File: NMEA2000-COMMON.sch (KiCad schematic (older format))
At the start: 55 parts, among them J2 CAN, SW1 PRG, SW2 INSTANCE, SW3 BUS, U1 MCP2551-I-P, U2 TMR-2-2411, U3 74HCT595, U4 74HCT595, U5 Teensy_4.0

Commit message: Update silk layer.
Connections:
- net 3V3 renamed +3V3
- no-connect marks 9 -> 17
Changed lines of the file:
@@
 Text Label 8650 5000 2    50   ~ 0
 MPX_SER
-Text Label 1150 3500 2    50   ~ 0
-3V3
 $Comp
 L Device:CP_Small C3
@@
 Text Label 2250 3500 0    50   ~ 0
 MPX_LATCH
-Text Label 1150 2700 2    50   ~ 0
-CH7
 Text Label 1150 2800 2    50   ~ 0
 CH6
@@
 	-1   0    0    -1
 $EndComp
+$Comp
+L power:+3V3 #PWR0103
+U 1 1 639236D5
+P 850 3500
+F 0 "#PWR0103" H 850 3350 50  0001 C CNN
+F 1 "+3V3" H 865 3673 50  0000 C CNN
+F 2 "" H 850 3500 50  0001 C CNN
+F 3 "" H 850 3500 50  0001 C CNN
+	1    850  3500
+	1    0    0    -1
+$EndComp
+Wire Wire Line
+	1150 3500 850  3500
+Text Label 1150 2700 2    50   ~ 0
+CH7
+NoConn ~ 1150 2700
+NoConn ~ 1150 2800
+NoConn ~ 1150 2900
+NoConn ~ 1150 3000
+NoConn ~ 1150 3100
+NoConn ~ 1150 3200
+NoConn ~ 1150 3300
+NoConn ~ 1150 3400
 $EndSCHEMATC

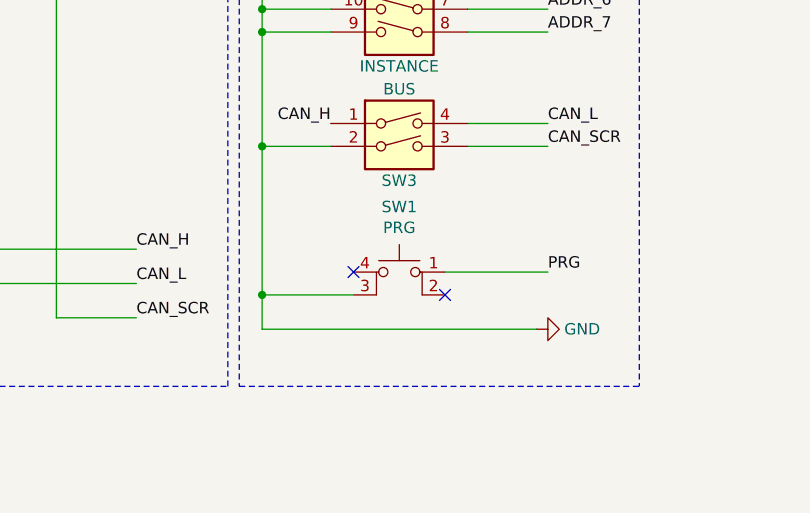
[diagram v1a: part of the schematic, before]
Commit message: Update PRG switch position
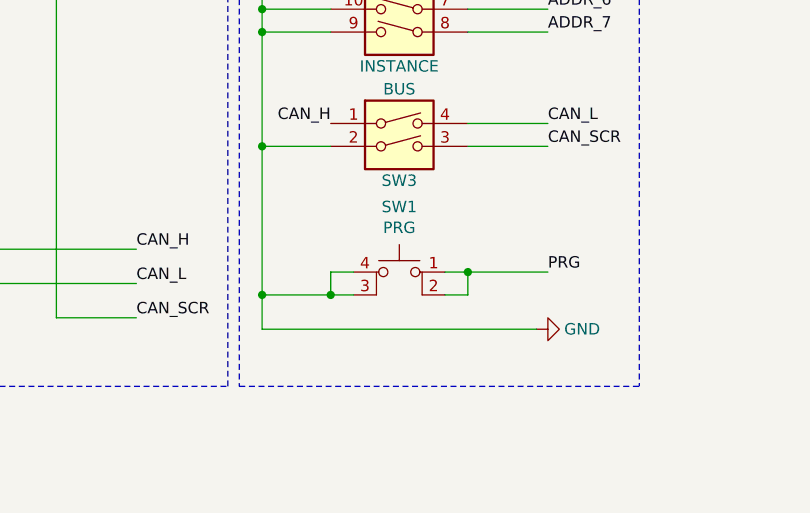
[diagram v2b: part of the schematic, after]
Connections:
- net GND: now also SW1.4 (A)
- net PRG: now also SW1.2
- no-connect marks 17 -> 15
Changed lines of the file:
@@
 	1200 6700 2350 6700
 Wire Wire Line
-	5950 7150 6400 7150
+	5950 7150 6050 7150
 Wire Wire Line
 	5150 7400 6350 7400
@@
 	-1   0    0    -1
 $EndComp
-NoConn ~ 5950 7250
-NoConn ~ 5550 7150
-Wire Wire Line
-	5550 7250 5150 7250
+Wire Wire Line
+	5550 7250 5450 7250
 $Comp
 L Device:LED D18
@@
 NoConn ~ 1150 3300
 NoConn ~ 1150 3400
+Wire Wire Line
+	5950 7250 6050 7250
+Wire Wire Line
+	6050 7250 6050 7150
+Connection ~ 6050 7150
+Wire Wire Line
+	6050 7150 6400 7150
+Wire Wire Line
+	5550 7150 5450 7150
+Wire Wire Line
+	5450 7150 5450 7250
+Connection ~ 5450 7250
+Wire Wire Line
+	5450 7250 5150 7250
 $EndSCHEMATC

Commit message: Revise INSTANCE
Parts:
- added C?: 100nF, Capacitor_SMD:C_0805_2012Metric, symbol Device:CP_Small
- added U?: 74LS165, symbol pdjr:74LS165
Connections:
- net labels added: D16, D17, D18, D19, D20, D21, D22, D23, D5, D6, D7, D8, INSTANCE_CLOCK, INSTANCE_CLOCK_ENABLE, INSTANCE_LOAD, INSTANCE_SERIAL, LED_CLOCK, LED_DATA, LED_LATCH, LED_SER
- net labels removed: CH0, CH1, CH2, CH3, CH4, CH5, CH6, CH7, MPX_CLOCK, MPX_DATA, MPX_LATCH, MPX_SER
- wire segments 205 -> 240
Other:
- moved on the sheet: SW2
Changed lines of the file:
@@
 	10350 3800 10450 3800
 Text Label 8650 3300 2    50   ~ 0
-MPX_DATA
+LED_DATA
 Text Label 8650 3500 2    50   ~ 0
-MPX_CLOCK
+LED_CLOCK
 Text Label 8650 3800 2    50   ~ 0
-MPX_LATCH
+LED_LATCH
 Wire Wire Line
 	9250 4400 9250 4500
@@
 L Switch:SW_DIP_x08 SW2
 U 1 1 633236F9
-P 5750 5800
-F 0 "SW2" H 5750 6350 50  0000 C CNN
-F 1 "INSTANCE" H 5750 5350 50  0000 C CNN
-F 2 "Package_DIP:DIP-16_W7.62mm" H 5750 5800 50  0001 C CNN
-F 3 "~" H 5750 5800 50  0001 C CNN
-	1    5750 5800
-	-1   0    0    -1
+P 6350 2000
+F 0 "SW2" H 6350 2550 50  0000 C CNN
+F 1 "INSTANCE" H 6350 1550 50  0000 C CNN
+F 2 "Package_DIP:DIP-16_W7.62mm" H 6350 2000 50  0001 C CNN
+F 3 "~" H 6350 2000 50  0001 C CNN
+	1    6350 2000
+	1    0    0    -1
 $EndComp
 Wire Wire Line
@@
 NoConn ~ 9650 5900
 Text Label 8650 5200 2    50   ~ 0
-MPX_CLOCK
+LED_CLOCK
 Text Label 8650 5500 2    50   ~ 0
-MPX_LATCH
+LED_LATCH
 Wire Wire Line
 	9250 6100 9250 6200
@@
 	10950 4000 10950 4500
 Text Label 9650 4200 0    50   ~ 0
-MPX_SER
+LED_SER
 Text Label 8650 5000 2    50   ~ 0
-MPX_SER
+LED_SER
 $Comp
 L Device:CP_Small C3
@@
 PRG
 Text Label 2250 3600 0    50   ~ 0
-MPX_CLOCK
+LED_CLOCK
 Text Label 2250 3400 0    50   ~ 0
-MPX_DATA
-Text Label 2250 3100 0    50   ~ 0
-ADDR_7
-Text Label 2250 3000 0    50   ~ 0
-ADDR_6
-Text Label 2250 2900 0    50   ~ 0
-ADDR_5
-Text Label 2250 2800 0    50   ~ 0
-ADDR_4
-Text Label 2250 2700 0    50   ~ 0
-ADDR_3
-Text Label 2250 2600 0    50   ~ 0
-ADDR_2
-Text Label 2250 2500 0    50   ~ 0
-ADDR_1
-Text Label 2250 2400 0    50   ~ 0
-ADDR_0
+LED_DATA
 Text Label 2250 3500 0    50   ~ 0
-MPX_LATCH
+LED_LATCH
 Text Label 1150 2800 2    50   ~ 0
-CH6
+D17
 Text Label 1150 2900 2    50   ~ 0
-CH5
+D18
 Text Label 1150 3000 2    50   ~ 0
-CH4
+D19
 Text Label 1150 3100 2    50   ~ 0
-CH3
+D20
 Text Label 1150 3200 2    50   ~ 0
-CH2
+D21
 Text Label 1150 3300 2    50   ~ 0
-CH1
+D22
 Text Label 1150 3400 2    50   ~ 0
-CH0
+D23
 NoConn ~ 1500 2200
 NoConn ~ 1600 2200
@@
 	1150 3500 850  3500
 Text Label 1150 2700 2    50   ~ 0
-CH7
+D16
 NoConn ~ 1150 2700
 NoConn ~ 1150 2800
@@
 Wire Wire Line
 	5450 7250 5150 7250
+Wire Wire Line
+	4100 1500 4000 1500
+Wire Wire Line
+	4600 1100 4150 1100
+$Comp
+L power:+3V3 #PWR?
+U 1 1 63A6B75E
+P 4150 1100
+F 0 "#PWR?" H 4150 950 50  0001 C CNN
+F 1 "+3V3" V 4150 1300 50  0000 C CNN
+F 2 "" H 4150 1100 50  0001 C CNN
+F 3 "" H 4150 1100 50  0001 C CNN
+	1    4150 1100
+	0    -1   -1   0
+$EndComp
+$Comp
+L power:GND #PWR?
+U 1 1 63A6CC25
+P 3950 2600
+F 0 "#PWR?" H 3950 2350 50  0001 C CNN
+F 1 "GND" V 3950 2400 50  0000 C CNN
+F 2 "" H 3950 2600 50  0001 C CNN
+F 3 "" H 3950 2600 50  0001 C CNN
+	1    3950 2600
+	0    1    1    0
+$EndComp
+Wire Wire Line
+	5100 1600 5200 1600
+Wire Wire Line
+	5100 1700 5200 1700
+Wire Wire Line
+	5100 1800 5200 1800
+Wire Wire Line
+	5100 1900 5200 1900
+Wire Wire Line
+	5100 2000 5200 2000
+Wire Wire Line
+	5100 2100 5200 2100
+Wire Wire Line
+	5100 2200 5200 2200
+Wire Wire Line
+	5100 2300 5200 2300
+Wire Wire Line
+	6750 2300 6650 2300
+Wire Wire Line
+	6750 2300 6750 2200
+Wire Wire Line
+	6750 2200 6650 2200
+Connection ~ 6750 2300
+Wire Wire Line
+	6750 2200 6750 2100
+Wire Wire Line
+	6750 2100 6650 2100
+Connection ~ 6750 2200
+Wire Wire Line
+	6750 2100 6750 2000
+Wire Wire Line
+	6750 2000 6650 2000
+Connection ~ 6750 2100
+Wire Wire Line
+	6750 2000 6750 1900
+Wire Wire Line
+	6750 1900 6650 1900
+Connection ~ 6750 2000
+Wire Wire Line
+	6750 1900 6750 1800
+Wire Wire Line
+	6750 1800 6650 1800
+Connection ~ 6750 1900
+Wire Wire Line
+	6750 1800 6750 1700
+Wire Wire Line
+	6750 1700 6650 1700
+Connection ~ 6750 1800
+Wire Wire Line
+	6750 1700 6750 1600
+Wire Wire Line
+	6750 1600 6650 1600
+Connection ~ 6750 1700
+$Comp
+L Device:CP_Small C?
+U 1 1 63C82001
+P 5150 1100
+F 0 "C?" V 5200 1200 50  0000 C CNN
+F 1 "100nF" V 5200 950 50  0000 C CNN
+F 2 "Capacitor_SMD:C_0805_2012Metric" H 5150 1100 50  0001 C CNN
+F 3 "~" H 5150 1100 50  0001 C CNN
+	1    5150 1100
+	0    -1   1    0
+$EndComp
+Wire Wire Line
+	6750 1600 6750 1100
+Wire Wire Line
+	5900 1100 5250 1100
+Connection ~ 6750 1600
+Wire Wire Line
+	5050 1100 4600 1100
+Connection ~ 4600 1100
+Wire Wire Line
+	4600 1100 4600 1200
+$Comp
+L pdjr:74LS165 U?
+U 1 1 63F7C7A4
+P 4600 2100
+F 0 "U?" H 4850 2850 50  0000 C CNN
+F 1 "74LS165" H 4300 2850 50  0000 C CNN
+F 2 "" H 4600 2100 50  0001 C CNN
+F 3 "https://www.ti.com/lit/ds/symlink/sn74ls165a.pdf" H 4600 2100 50  0001 C CNN
+	1    4600 2100
+	-1   0    0    -1
+$EndComp
+Wire Wire Line
+	4600 2600 5900 2550
+Wire Wire Line
+	6750 2600 6750 2300
+Wire Wire Line
+	3950 2600 4600 2600
+Connection ~ 4600 2600
+Text Label 4000 2000 2    50   ~ 0
+INSTANCE_CLOCK
+Text Label 4000 1500 2    50   ~ 0
+INSTANCE_SERIAL
+Wire Wire Line
+	4100 2000 4000 2000
+Text Label 4000 2100 2    50   ~ 0
+INSTANCE_CLOCK_ENABLE
+Wire Wire Line
+	4100 2100 4000 2100
+Text Label 4000 1800 2    50   ~ 0
+INSTANCE_LOAD
+Wire Wire Line
+	4100 1800 4000 1800
+Text Label 2250 2400 0    50   ~ 0
+INSTANCE_LOAD
+Text Label 2250 2500 0    50   ~ 0
+INSTANCE_CLOCK
+Text Label 2250 2600 0    50   ~ 0
+INSTANCE_SERIAL
+Text Label 2250 2700 0    50   ~ 0
+INSTANCE_CLOCK_ENABLE
+Text Label 2250 2800 0    50   ~ 0
+D8
+Text Label 2250 2900 0    50   ~ 0
+D7
+Text Label 2250 3000 0    50   ~ 0
+D6
+Text Label 2250 3100 0    50   ~ 0
+D5
 $EndSCHEMATC

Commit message: PISI update
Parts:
- added R101, R102, R103, R104, R105, R106, R107, R108: 4K7 0.125W, Resistor_SMD:R_0805_2012Metric, symbol Device:R
- U101: renamed from U?; footprint (none) -> Package_SO:SO-16_3.9x9.9mm_P1.27mm
- gave numbers to parts that had none: 1
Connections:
- net labels added: INSTANCE_CE, INSTANCE_CP, INSTANCE_PL, INSTANCE_Q7
- net labels removed: ADDR_0, ADDR_1, ADDR_2, ADDR_3, ADDR_4, ADDR_5, ADDR_6, ADDR_7, INSTANCE_CLOCK, INSTANCE_CLOCK_ENABLE, INSTANCE_LOAD, INSTANCE_SERIAL
- wire segments 240 -> 250
- no-connect marks 15 -> 19
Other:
- moved on the sheet: C101, SW2, U101

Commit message: Tidy up
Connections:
- net GND: now also SW3.4; no longer SW3.2
- net CAN_H: no longer names the net of SW3.1
- net CAN_H: now also J2.5 (Pin_5); no longer R2.2
- net CAN_L: no longer names the net of J2.4 (Pin_4), U1.6 (CANL)
- net CAN_L: now also SW3.3; no longer SW3.4
- removed net CAN_SCR: J2.5 (Pin_5), SW3.3
- new net: R2.2, SW3.2
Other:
- note removed: "CONFIGURATION"
- moved on the sheet: R2, SW1, SW3
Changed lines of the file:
@@
 Text Label 650  7100 0    50   ~ 0
 CAN_TX
-Wire Wire Line
-	4250 7350 4600 7350
 Text Notes 600  5200 0    50   ~ 10
 POWER SUPPLY & CAN INTERFACE
-Text Label 4600 7350 0    50   ~ 0
-CAN_SCR
 Wire Wire Line
 	3350 5800 3450 5800
@@
 L Device:R R2
 U 1 1 63360130
-P 3800 7050
-F 0 "R2" V 3700 7100 50  0000 R CNN
-F 1 "120R 0.5W" V 3800 7050 20  0000 C CNN
-F 2 "Resistor_THT:R_Axial_DIN0207_L6.3mm_D2.5mm_P7.62mm_Horizontal" V 3730 7050 50  0001 C CNN
-F 3 "~" H 3800 7050 50  0001 C CNN
-	1    3800 7050
-	0    -1   -1   0
-$EndComp
-Text Label 4600 7050 0    50   ~ 0
-CAN_H
-Wire Wire Line
-	4600 7050 3950 7050
-Text Label 4600 7200 0    50   ~ 0
-CAN_L
-Wire Wire Line
-	3350 6700 3550 6700
-Wire Wire Line
-	3650 7050 3550 7050
-Wire Wire Line
-	3550 7050 3550 6700
-Connection ~ 3550 6700
-Wire Wire Line
-	3550 6700 3900 6700
-Wire Wire Line
-	4600 7200 3450 7200
-Wire Wire Line
-	3450 7200 3450 6900
-Connection ~ 3450 6900
-Wire Wire Line
-	3450 6900 4000 6900
-Wire Wire Line
-	3350 6900 3450 6900
-Text Label 5450 6500 2    50   ~ 0
-CAN_H
-Text Label 6400 6500 0    50   ~ 0
-CAN_L
+P 4000 6700
+F 0 "R2" V 3900 6750 50  0000 R CNN
+F 1 "120R 0.5W" V 4000 6700 20  0000 C CNN
+F 2 "Resistor_THT:R_Axial_DIN0207_L6.3mm_D2.5mm_P7.62mm_Horizontal" V 3930 6700 50  0001 C CNN
+F 3 "~" H 4000 6700 50  0001 C CNN
+	1    4000 6700
+	0    -1   -1   0
+$EndComp
 $Comp
 L Connector:Screw_Terminal_01x05 J2
@@
 	-1   0    0    1
 $EndComp
-Text Label 6400 6600 0    50   ~ 0
-CAN_SCR
 $Comp
 L Switch:SW_DIP_x02 SW3
 U 1 1 62A67242
-P 5750 6600
-F 0 "SW3" H 5750 6450 50  0000 C CNN
-F 1 "BUS" H 5750 6850 50  0000 C CNN
-F 2 "Package_DIP:DIP-4_W7.62mm_LongPads" H 5750 6600 50  0001 C CNN
-F 3 "~" H 5750 6600 50  0001 C CNN
-	1    5750 6600
+P 4550 6700
+F 0 "SW3" H 4550 6550 50  0000 C CNN
+F 1 "BUS" H 4550 6950 50  0000 C CNN
+F 2 "Package_DIP:DIP-4_W7.62mm_LongPads" H 4550 6700 50  0001 C CNN
+F 3 "~" H 4550 6700 50  0001 C CNN
+	1    4550 6700
 	1    0    0    -1
 $EndComp
@@
 	1    0    0    -1
 $EndComp
-Wire Wire Line
-	5150 6600 5450 6600
 Connection ~ 9250 3000
 Wire Wire Line
@@
 Wire Wire Line
 	10000 3000 10950 3000
-Text Label 6400 7150 0    50   ~ 0
+Text Label 6600 3250 2    50   ~ 0
 PRG
 $Comp
@@
 Wire Wire Line
 	950  5800 2000 5800
-Wire Notes Line
-	5050 5200 6800 5200
-Text Notes 5050 5200 0    50   ~ 10
-CONFIGURATION
 Wire Notes Line
 	11050 2400 11050 6350
@@
 Wire Notes Line
 	600  7650 5000 7650
-Wire Notes Line
-	5050 7650 6800 7650
-Wire Notes Line
-	6800 5200 6800 7650
-Wire Notes Line
-	5050 5200 5050 7650
 $Comp
 L power:GND #PWR014
 U 1 1 63724529
-P 6350 7400
-F 0 "#PWR014" H 6350 7150 50  0001 C CNN
-F 1 "GND" V 6350 7200 50  0000 C CNN
-F 2 "" H 6350 7400 50  0001 C CNN
-F 3 "" H 6350 7400 50  0001 C CNN
-	1    6350 7400
-	0    -1   -1   0
-$EndComp
-Wire Wire Line
-	6050 6500 6400 6500
-Wire Wire Line
-	6050 6600 6400 6600
+P 4600 3550
+F 0 "#PWR014" H 4600 3300 50  0001 C CNN
+F 1 "GND" V 4600 3350 50  0000 C CNN
+F 2 "" H 4600 3550 50  0001 C CNN
+F 3 "" H 4600 3550 50  0001 C CNN
+	1    4600 3550
+	0    1    -1   0
+$EndComp
 NoConn ~ -3250 8100
 $Comp
@@
 	1200 6700 2350 6700
 Wire Wire Line
-	5950 7150 6050 7150
-Wire Wire Line
-	5150 7400 6350 7400
+	6800 3250 6700 3250
+Wire Wire Line
+	7450 3550 5300 3550
 Connection ~ 1400 7550
 Wire Wire Line
@@
 L Switch:SW_MEC_5E SW1
 U 1 1 638DE6DD
-P 5750 7250
-F 0 "SW1" H 5750 7635 50  0000 C CNN
-F 1 "PRG" H 5750 7544 50  0000 C CNN
-F 2 "Button_Switch_THT:SW_TH_Tactile_Omron_B3F-10xx" H 5750 7550 50  0001 C CNN
-F 3 "http://www.apem.com/int/index.php?controller=attachment&id_attachment=1371" H 5750 7550 50  0001 C CNN
-	1    5750 7250
-	-1   0    0    -1
-$EndComp
-Wire Wire Line
-	5550 7250 5450 7250
+P 7000 3350
+F 0 "SW1" H 7000 3600 50  0000 C CNN
+F 1 "PRG" H 7000 3350 50  0000 C CNN
+F 2 "Button_Switch_THT:SW_TH_Tactile_Omron_B3F-10xx" H 7000 3650 50  0001 C CNN
+F 3 "http://www.apem.com/int/index.php?controller=attachment&id_attachment=1371" H 7000 3650 50  0001 C CNN
+	1    7000 3350
+	1    0    0    -1
+$EndComp
 $Comp
 L Device:LED D18
@@
 	3850 5400 4350 5400
 Wire Wire Line
-	4350 5800 4250 5800
-Wire Wire Line
-	4250 5800 4250 7350
-Wire Wire Line
-	4350 5700 4000 5700
-Wire Wire Line
-	4000 5700 4000 6900
-Wire Wire Line
-	3900 5600 4350 5600
-Wire Wire Line
-	3900 5600 3900 6700
+	4350 5700 3750 5700
+Wire Wire Line
+	3750 5700 3750 6900
+Wire Wire Line
+	3650 5600 4350 5600
+Wire Wire Line
+	3650 5600 3650 6700
 Text Notes 4600 5450 0    50   ~ 0
 NET_S
@@
 Wire Wire Line
 	4600 5200 4650 5200
-Wire Wire Line
-	5150 6600 5150 7250
-Connection ~ 5150 7250
-Wire Wire Line
-	5150 7250 5150 7400
 $Comp
 L pdjr:TMR-2-2411 U2
@@
 NoConn ~ 1150 3400
 Wire Wire Line
-	5950 7250 6050 7250
-Wire Wire Line
-	6050 7250 6050 7150
-Connection ~ 6050 7150
-Wire Wire Line
-	6050 7150 6400 7150
-Wire Wire Line
-	5550 7150 5450 7150
-Wire Wire Line
-	5450 7150 5450 7250
-Connection ~ 5450 7250
-Wire Wire Line
-	5450 7250 5150 7250
+	6800 3350 6700 3350
+Wire Wire Line
+	6700 3350 6700 3250
+Connection ~ 6700 3250
+Wire Wire Line
+	6700 3250 6600 3250
 Wire Wire Line
 	4800 2000 4600 2000
 Wire Wire Line
-	5300 1600 4850 1600
-$Comp
-L power:GND #PWR0104
-U 1 1 63A6CC25
-P 4650 3300
-F 0 "#PWR0104" H 4650 3050 50  0001 C CNN
-F 1 "GND" V 4650 3100 50  0000 C CNN
-F 2 "" H 4650 3300 50  0001 C CNN
-F 3 "" H 4650 3300 50  0001 C CNN
-	1    4650 3300
-	0    1    1    0
-$EndComp
+	5300 1600 4600 1600
 Wire Wire Line
 	7450 2800 7300 2800
@@
 U 1 1 63C82001
 P 7000 1600
-F 0 "C101" V 7050 1700 50  0000 C CNN
+F 0 "C101" V 7050 1750 50  0000 C CNN
 F 1 "100nF" V 7050 1450 50  0000 C CNN
 F 2 "Capacitor_SMD:C_0805_2012Metric" H 7000 1600 50  0001 C CNN
@@
 U 1 1 6394A88D
 P 6000 1850
-F 0 "R102" H 6000 1700 50  0000 R CNN
+F 0 "R102" V 5950 2150 50  0000 R CNN
 F 1 "4K7 0.125W" V 6000 1850 20  0000 C CNN
 F 2 "Resistor_SMD:R_0805_2012Metric" V 5930 1850 50  0001 C CNN
@@
 U 1 1 6394F8BB
 P 6100 1850
-F 0 "R103" H 6100 1700 50  0000 R CNN
+F 0 "R103" V 6050 2150 50  0000 R CNN
 F 1 "4K7 0.125W" V 6100 1850 20  0000 C CNN
 F 2 "Resistor_SMD:R_0805_2012Metric" V 6030 1850 50  0001 C CNN
@@
 U 1 1 6395000A
 P 6200 1850
-F 0 "R104" H 6200 1700 50  0000 R CNN
+F 0 "R104" V 6150 2150 50  0000 R CNN
 F 1 "4K7 0.125W" V 6200 1850 20  0000 C CNN
 F 2 "Resistor_SMD:R_0805_2012Metric" V 6130 1850 50  0001 C CNN
@@
 U 1 1 63950611
 P 6300 1850
-F 0 "R105" H 6300 1700 50  0000 R CNN
+F 0 "R105" V 6250 2150 50  0000 R CNN
 F 1 "4K7 0.125W" V 6300 1850 20  0000 C CNN
 F 2 "Resistor_SMD:R_0805_2012Metric" V 6230 1850 50  0001 C CNN
@@
 U 1 1 63950BCD
 P 6400 1850
-F 0 "R106" H 6400 1700 50  0000 R CNN
+F 0 "R106" V 6350 2150 50  0000 R CNN
 F 1 "4K7 0.125W" V 6400 1850 20  0000 C CNN
 F 2 "Resistor_SMD:R_0805_2012Metric" V 6330 1850 50  0001 C CNN
@@
 U 1 1 639511BB
 P 6500 1850
-F 0 "R107" H 6500 1700 50  0000 R CNN
+F 0 "R107" V 6450 2150 50  0000 R CNN
 F 1 "4K7 0.125W" V 6500 1850 20  0000 C CNN
 F 2 "Resistor_SMD:R_0805_2012Metric" V 6430 1850 50  0001 C CNN
@@
 U 1 1 63951797
 P 6600 1850
-F 0 "R108" H 6600 1700 50  0000 R CNN
+F 0 "R108" V 6550 2150 50  0000 R CNN
 F 1 "4K7 0.125W" V 6600 1850 20  0000 C CNN
 F 2 "Resistor_SMD:R_0805_2012Metric" V 6530 1850 50  0001 C CNN
@@
 U 1 1 63B2611A
 P 5900 1850
-F 0 "R101" H 5900 1700 50  0000 R CNN
+F 0 "R101" V 5850 2150 50  0000 R CNN
 F 1 "4K7 0.125W" V 5900 1850 20  0000 C CNN
 F 2 "Resistor_SMD:R_0805_2012Metric" V 5830 1850 50  0001 C CNN
@@
 $EndComp
 Wire Wire Line
-	5300 3300 5300 3100
-Wire Wire Line
-	7450 2800 7450 3300
-Wire Wire Line
-	4650 3300 5300 3300
-Connection ~ 5300 3300
+	5300 3550 5300 3100
 Wire Wire Line
 	7100 1600 7450 1600
@@
 L power:+5V #PWR0105
 U 1 1 63D83162
-P 4850 1600
-F 0 "#PWR0105" H 4850 1450 50  0001 C CNN
-F 1 "+5V" V 4850 1750 50  0000 L CNN
-F 2 "" H 4850 1600 50  0001 C CNN
-F 3 "" H 4850 1600 50  0001 C CNN
-	1    4850 1600
-	0    -1   -1   0
-$EndComp
-Wire Wire Line
-	5300 3300 7450 3300
+P 4600 1600
+F 0 "#PWR0105" H 4600 1450 50  0001 C CNN
+F 1 "+5V" V 4600 1750 50  0000 L CNN
+F 2 "" H 4600 1600 50  0001 C CNN
+F 3 "" H 4600 1600 50  0001 C CNN
+	1    4600 1600
+	0    -1   -1   0
+$EndComp
 Connection ~ 5900 2800
 Wire Wire Line
@@
 Connection ~ 9250 4500
 Connection ~ 8750 4500
+Connection ~ 7450 3350
+Wire Wire Line
+	7450 3350 7450 3550
+Wire Wire Line
+	7450 2800 7450 3250
+Connection ~ 7450 3250
+Wire Wire Line
+	7450 3250 7450 3350
+Wire Wire Line
+	7200 3250 7450 3250
+Wire Wire Line
+	7200 3350 7450 3350
+Connection ~ 5300 3550
+Wire Wire Line
+	5300 3550 4600 3550
+Connection ~ 2850 7550
+Wire Wire Line
+	3650 6700 3850 6700
+Connection ~ 3650 6700
+Wire Wire Line
+	4150 6700 4250 6700
+Wire Wire Line
+	3350 6700 3650 6700
+Wire Wire Line
+	4950 6900 4950 6700
+Wire Wire Line
+	4950 6700 4850 6700
+Wire Wire Line
+	3750 6900 4950 6900
+Connection ~ 3750 6900
+Wire Wire Line
+	3350 6900 3750 6900
+Wire Wire Line
+	4150 5800 4150 6600
+Wire Wire Line
+	4150 6600 4250 6600
+Wire Wire Line
+	4150 5800 4350 5800
+Wire Wire Line
+	4850 6600 5050 6600
+Wire Wire Line
+	5050 6600 5050 7550
+Wire Wire Line
+	2850 7550 5050 7550
 $EndSCHEMATC

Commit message: Tidy up
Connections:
- no-connect marks 19 -> 21
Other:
- note removed: "DISPLAY"
- moved on the sheet: C1, C101, C2, C3, C4, C5, D1, D18, D19, D2, D20, D21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
